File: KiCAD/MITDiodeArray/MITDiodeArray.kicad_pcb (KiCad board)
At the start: 2 copper layers, 30 x 30 mm, 23 parts

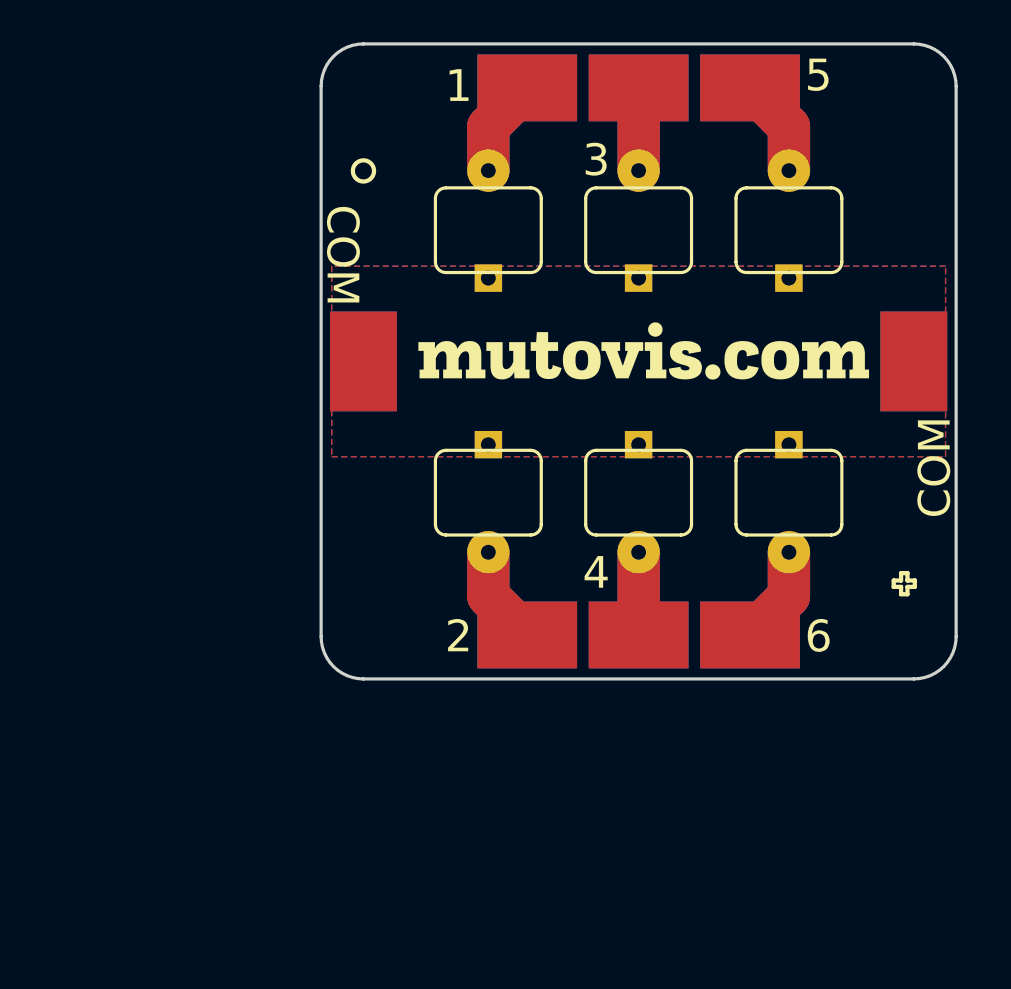
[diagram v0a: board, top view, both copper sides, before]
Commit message: adapter and photodiode board for mit
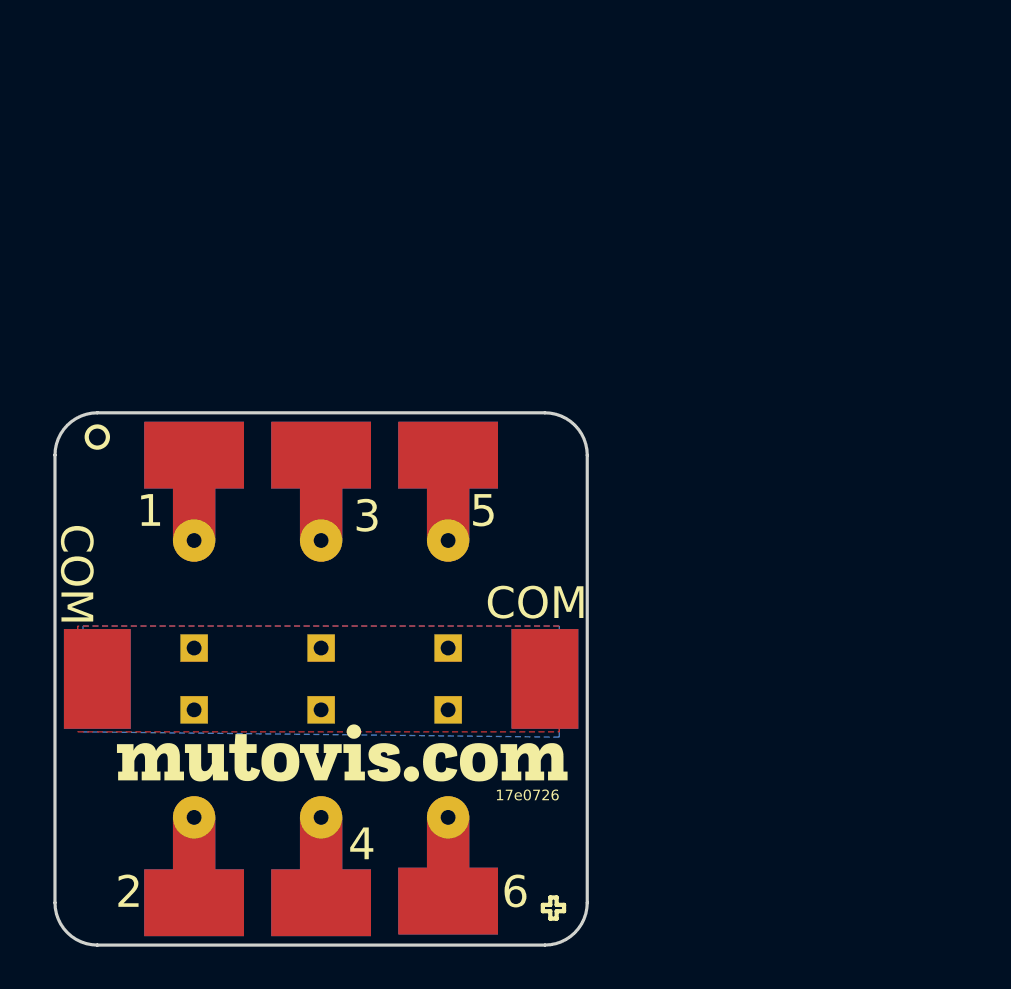
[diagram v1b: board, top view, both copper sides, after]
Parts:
- moved D5 23.8 mm to (6.00, -1.46)
- moved text 23.7 mm to (1.00, 3.50)
- moved W12 23.4 mm to (-6.00, -10.6)
- moved W2 23.4 mm to (-6.00, -10.6)
- moved D3 23.0 mm to (0.00, -1.46)
- moved W10 23.0 mm to (10.6, 0.00)
- moved W20 23.0 mm to (10.6, 0.00)
- moved W14 22.9 mm to (0.00, -10.6)
- moved W4 22.9 mm to (0.00, -10.6)
- moved W16 22.5 mm to (6.00, -10.6)
- moved W6 22.5 mm to (6.00, -10.6)
- moved D1 22.3 mm to (-6.00, -1.46)
- moved D6 20.4 mm to (6.00, 1.46)
- moved W13 20.2 mm to (-6.00, 10.6)
- moved W3 20.2 mm to (-6.00, 10.6)
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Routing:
- net Net-(D6-Pad2): track 9.34 -> 7.91 mm
- net Net-(D5-Pad2): track 9.34 -> 8.07 mm
- net Net-(D1-Pad2): track 9.34 -> 8.07 mm
- net Net-(D2-Pad2): track 9.34 -> 8.07 mm
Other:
- board size 30 x 30 mm -> 25.1 x 25.1 mm

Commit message: update silk
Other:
- board text added: "8694043"
- board text removed: "17e0726"
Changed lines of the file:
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@@
   )
   (setup
-    (last_trace_width 2)
+    (last_trace_width 0.25)
     (user_trace_width 1)
     (user_trace_width 2)
@@
     (effects (font (size 1.5 1.5) (thickness 0.3)))
   )
-  (gr_text 17e0726 (at 9.75 5.5) (layer F.SilkS)
+  (gr_text 8694043 (at 9.75 5.5) (layer F.SilkS)
     (effects (font (size 0.5 0.5) (thickness 0.125)))
   )

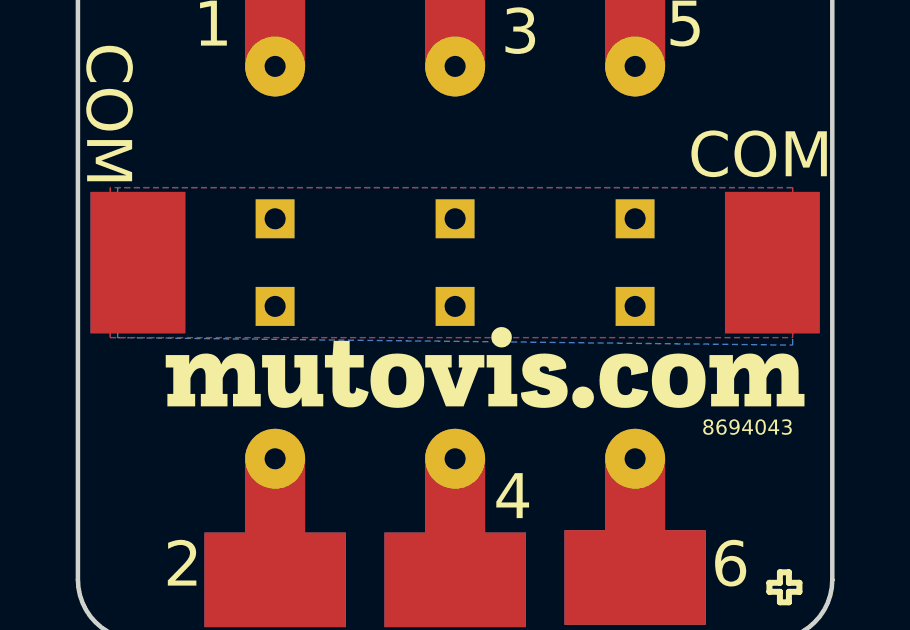
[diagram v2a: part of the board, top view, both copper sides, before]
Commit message: clean up mit springpin board names
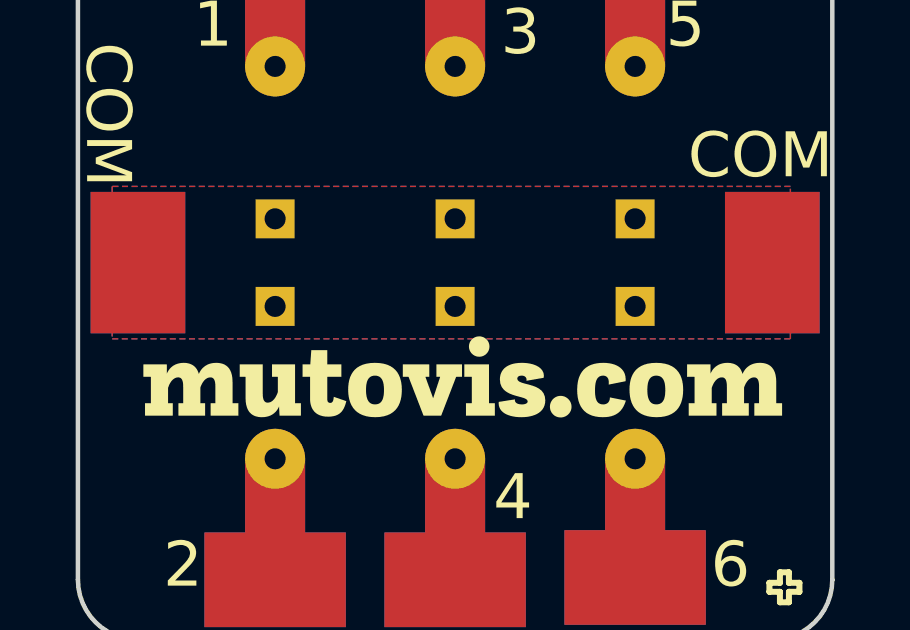
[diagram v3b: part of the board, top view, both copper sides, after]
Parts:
- removed the text at (1.00, 3.50)
- added text: G***, logo:text, F.Cu at (0.25, 3.81)
- added text: G***, logo:text, B.Cu at (0.25, 4.06)
